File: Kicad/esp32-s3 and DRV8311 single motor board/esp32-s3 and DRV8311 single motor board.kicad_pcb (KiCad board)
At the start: 4 copper layers, 38.8 x 42.1 mm, 74 parts, among them J1 JST SH SM04B, J2 JST SH SM06B, J3 Molex_PicoBlade_53048-0310 Ho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, J4 Conn_01x02_Pin, Q1 NMOS, sir404dp, Q2 NMOS, Q3 PMOS,Si7157DP, Q4 PMOS, SW1 SW_Push, U1 STM32G070CBTr, U2 DRV8311HRRWR, U3 BQ298012RUGT, U4 BQ25060, Y1 ABM8-16.000MHZ-10-1-U-T

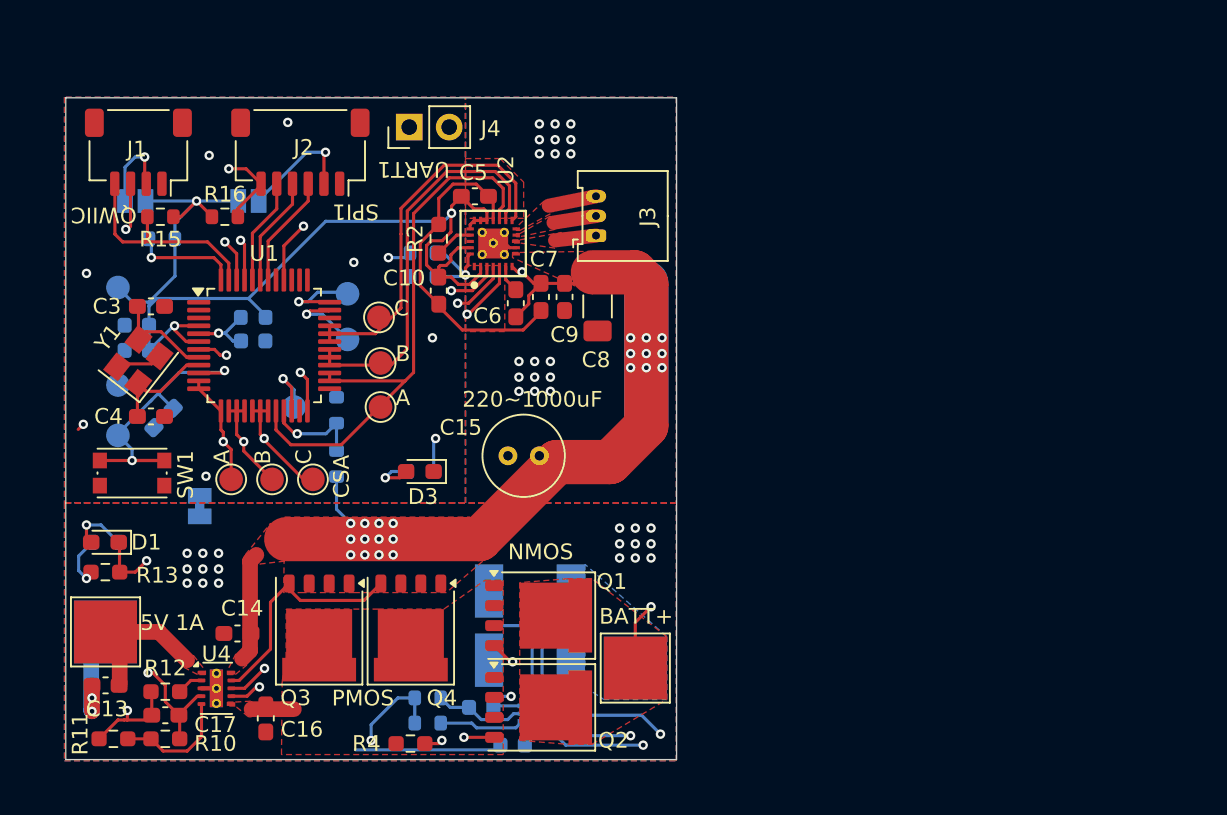
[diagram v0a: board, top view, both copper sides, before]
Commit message: Finished schematic and fixed DRC errors
Now I'm moving on to layout.
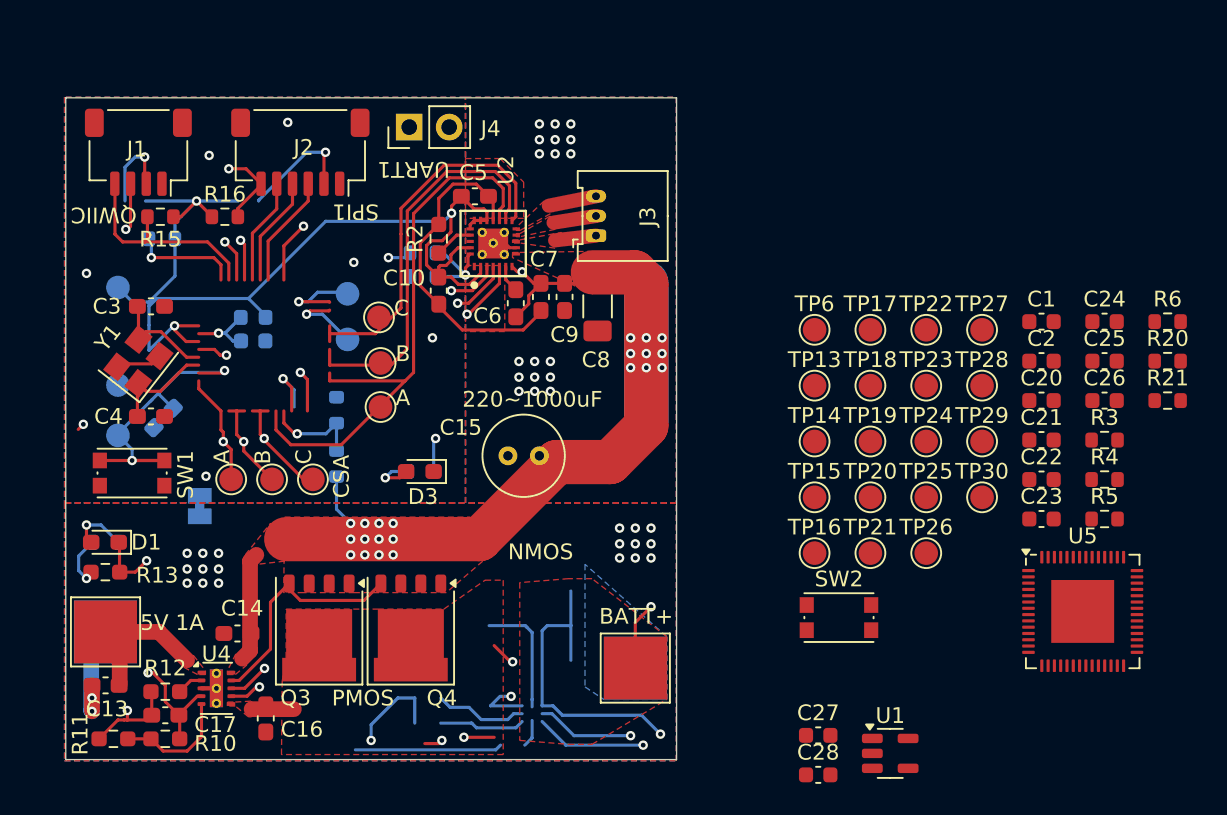
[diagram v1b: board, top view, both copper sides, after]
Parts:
- removed C11: 8nF, Capacitor_SMD:C_0603_1608Metric
- removed C12: 1uF, 16v, Capacitor_SMD:C_0603_1608Metric
- removed JP1, JP2: VCC, Jumper:SolderJumper-2_P1.3mm_Bridged_Pad1.0x1.5mm
- removed Q1: NMOS, sir404dp, Package_DFN_QFN:PQFN-8-EP_6x5mm_P1.27mm_Generic
- removed Q2: NMOS, Package_DFN_QFN:PQFN-8-EP_6x5mm_P1.27mm_Generic
- removed R7: Vishay WSLF2512, 1%, 300uOhm, vishay_wslf:RES_WSLF2512_VIS-M
- removed U3: BQ298012RUGT, bq298rugt:RUG8_TEX
- added C20: 0.1uF, Capacitor_SMD:C_0603_1608Metric, F.Cu at (184.7, 107.4)
- added C21: 1uF, Capacitor_SMD:C_0603_1608Metric, F.Cu at (184.7, 109.9)
- added C22: 0.1uF, Capacitor_SMD:C_0603_1608Metric, F.Cu at (184.7, 112.4)
- added C23: 0.1uF, Capacitor_SMD:C_0603_1608Metric, F.Cu at (184.7, 114.9)
- added C24: 1uF, Capacitor_SMD:C_0603_1608Metric, F.Cu at (188.7, 102.4)
- added C25: 0.1uF, Capacitor_SMD:C_0603_1608Metric, F.Cu at (188.7, 104.9)
- added C26: 22uF, Capacitor_SMD:C_0603_1608Metric, F.Cu at (188.7, 107.4)
- added C27: 22uf, Capacitor_SMD:C_0603_1608Metric, F.Cu at (170.5, 128.7)
- added C28: 22uf, Capacitor_SMD:C_0603_1608Metric, F.Cu at (170.5, 131.2)
- added R20: 10k, Resistor_SMD:R_0603_1608Metric, F.Cu at (192.8, 104.9)
- added R21: 100k, Resistor_SMD:R_0603_1608Metric, F.Cu at (192.8, 107.4)
- added SW2: SW_Push, Button_Switch_SMD:SW_Push_1P1T_NO_CK_KMR2, F.Cu at (171.8, 121.2)
- added TP13: TestPoint, TestPoint:TestPoint_Pad_D1.5mm, F.Cu at (170.3, 106.4)
- added TP14: ~, TestPoint:TestPoint_Pad_D1.5mm, F.Cu at (170.3, 110.0)
- added TP15: ~, TestPoint:TestPoint_Pad_D1.5mm, F.Cu at (170.3, 113.5)
- added TP16: ~, TestPoint:TestPoint_Pad_D1.5mm, F.Cu at (170.3, 117.1)
- added TP17: ~, TestPoint:TestPoint_Pad_D1.5mm, F.Cu at (173.8, 102.9)
- added TP18: ~, TestPoint:TestPoint_Pad_D1.5mm, F.Cu at (173.8, 106.4)
- added TP19: ~, TestPoint:TestPoint_Pad_D1.5mm, F.Cu at (173.8, 110.0)
- added TP20: ~, TestPoint:TestPoint_Pad_D1.5mm, F.Cu at (173.8, 113.5)
- added TP21: ~, TestPoint:TestPoint_Pad_D1.5mm, F.Cu at (173.8, 117.1)
- added TP22: ~, TestPoint:TestPoint_Pad_D1.5mm, F.Cu at (177.4, 102.9)
- added TP23: ~, TestPoint:TestPoint_Pad_D1.5mm, F.Cu at (177.4, 106.4)
- added TP24: ~, TestPoint:TestPoint_Pad_D1.5mm, F.Cu at (177.4, 110.0)
- added TP25: ~, TestPoint:TestPoint_Pad_D1.5mm, F.Cu at (177.4, 113.5)
- added TP26: ~, TestPoint:TestPoint_Pad_D1.5mm, F.Cu at (177.4, 117.1)
- added TP27: ~, TestPoint:TestPoint_Pad_D1.5mm, F.Cu at (180.9, 102.9)
- added TP28: ~, TestPoint:TestPoint_Pad_D1.5mm, F.Cu at (180.9, 106.4)
- added TP29: ~, TestPoint:TestPoint_Pad_D1.5mm, F.Cu at (180.9, 110.0)
- added TP30: ~, TestPoint:TestPoint_Pad_D1.5mm, F.Cu at (180.9, 113.5)
- added U5: ESP32-S3, Package_DFN_QFN:QFN-56-1EP_7x7mm_P0.4mm_EP4x4mm, F.Cu at (187.3, 120.8)
- C1: value 0.1uF -> 1uF; moved to F.Cu
- C18: value 0.1uF -> 1uF
- C2: value 4.7uF -> 1uF; moved to F.Cu
- C3, C4: value 12pF -> 16pF
- J2: value JST SH SM06B -> 7 pin FPC 0.3mm
- R3: value 20ohm -> 33ohm; moved to F.Cu
- R4: value 2k -> 33ohm; footprint Resistor_SMD:R_0603_1608Metric_Pad0.98x0.95mm_HandSolder -> Resistor_SMD:R_0603_1608Metric
- R5: value 300ohm -> 33ohm; moved to F.Cu
- R6: value Same, 1000uOhm -> 33ohm; footprint vishay_wslf:RES_WSLF2512_VIS-M -> Resistor_SMD:R_0603_1608Metric; moved to F.Cu
- TP6: value TestPoint -> ~; moved to F.Cu
- U1: value STM32G070CBTr -> AP2112K-3.3; footprint Package_QFP:LQFP-48_7x7mm_P0.5mm -> Package_TO_SOT_SMD:SOT-23-5
- Y1: value ABM8-16.000MHZ-10-1-U-T -> 40mhz, 10ppm
- moved C2 57.6 mm to (184.7, 104.9), turned to 0 degrees
- moved C1 57.6 mm to (184.7, 102.4), turned to 0 degrees
- moved U1 47.5 mm to (175.1, 129.8)
- moved R4 47.2 mm to (188.7, 112.4)
- moved R3 46.7 mm to (188.7, 109.9)
- moved R5 44.5 mm to (188.7, 114.9)
- moved R6 44.0 mm to (192.8, 102.4), turned to 0 degrees
- moved TP6 33.5 mm to (170.3, 102.9), turned to 0 degrees
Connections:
- C10 pad 2: VDD -> /DRV8311/RegulatorOut
- C16 pad 2: /PSU/Pack+ -> /PSU/BATT+
- C19 pad 1: GND -> Net-(C19-Pad1)
- C19 pad 2: Net-(U1-VREF+) -> GND
- C3 pad 1: Net-(U1-PF0) -> Net-(U5-XTAL_P)
- C4 pad 1: Net-(U1-PF1) -> Net-(U5-XTAL_N)
- C5 pad 2: VDD -> /DRV8311/RegulatorOut
- FB1 pad 1: Net-(U1-VREF+) -> Net-(C19-Pad1)
- H2 pad 1: /PSU/BATT- -> GNDPWR
- J1 pad 2: Net-(J1-Pin_2) -> VDD
- J2 pad 2: Net-(J2-Pin_2) -> VDD
- J4 pad 1: /USART1_TX -> /UART0_TX
- J4 pad 2: /USART1_RX -> /UART0_RX
- Q3 pad 5: /PSU/Pack+ -> /PSU/BATT+
- Q4 pad 5: /PSU/Pack+ -> /PSU/BATT+
- R17 pad 1: /ADC10/VBATT -> /VBATT
- R18 pad 2: /ADC10/VBATT -> /VBATT
- R3 pad 1: /PSU/BATT+ -> Net-(U5-MTDI)
- R3 pad 2: Net-(U3-BAT) -> /MISO1
- R4 pad 1: /PSU/Pack+ -> Net-(U5-MTDO)
- R4 pad 2: Net-(U3-PACK) -> /MOSI1
- R5 pad 1: /PSU/BATT+ -> Net-(U5-MTCK)
- R5 pad 2: Net-(U3-VDD) -> /SCK1
- R6 pad 1: /PSU/BATT- -> /CS1
- R6 pad 2: GNDPWR -> Net-(U5-GPIO12)
- TP1 pad 1: /NRST -> /CS0
- TP2 pad 1: /SWD -> /SCK1
- TP3 pad 1: /SWC -> /MOSI1
- TP6 pad 1: /ADC11 -> Net-(U5-SPICLK_P)
- U1 pad 1: /CS2 -> /MOTORPWR
- U1 pad 2: /CS3 -> GND
- U1 pad 3: /CS4 -> /MOTORPWR
- U1 pad 4: VDD -> unconnected-(U1-NC-Pad4)
- U1 pad 5: Net-(U1-VREF+) -> VDD
- U2 pad 17: VDD -> /DRV8311/RegulatorOut
- U2 pad 18: VDD -> /DRV8311/RegulatorOut
- U2 pad 19: VDD -> /DRV8311/RegulatorOut
- U2 pad 2: VDD -> /DRV8311/RegulatorOut
- U2 pad 20: VDD -> /DRV8311/RegulatorOut
- U2 pad 23: VDD -> /DRV8311/RegulatorOut
- U4 pad 6: /PSU/Pack+ -> /PSU/BATT+
- Y1 pad 1: Net-(U1-PF1) -> Net-(U5-XTAL_N)
- Y1 pad 3: Net-(U1-PF0) -> Net-(U5-XTAL_P)
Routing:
- net (no net): track 0.00 -> 69.5 mm, vias 0 -> 6
- net /PSU/BATT-: track 34.2 -> 0.00 mm, vias 2 -> 0
- net GNDPWR: track 26.1 -> 60.3 mm, vias 38 -> 40
- net Net-(Q1-G): track 27.7 -> 0.00 mm, vias 3 -> 0
- net /USART1_RX: track 20.4 -> 0.00 mm, vias 1 -> 0
- net /UART0_RX: track 0.00 -> 20.4 mm, vias 0 -> 1
- net Net-(U3-PACK): track 20.0 -> 0.00 mm, vias 2 -> 0
- net /USART1_TX: track 17.5 -> 0.00 mm, vias 1 -> 0
- net /UART0_TX: track 0.00 -> 17.5 mm, vias 0 -> 1
- net VDD: track 69.7 -> 82.8 mm, vias 3 -> 5
- net Net-(J2-Pin_2): track 7.60 -> 0.00 mm, vias 1 -> 0
- net Net-(U5-XTAL_P): track 0.00 -> 7.05 mm
- net Net-(U1-PF0): track 7.05 -> 0.00 mm
- net Net-(U5-XTAL_N): track 0.00 -> 6.88 mm
- net Net-(U1-PF1): track 6.88 -> 0.00 mm
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- removed copper zone on B.Cu, net /PSU/BATT-
- removed copper zone on F.Cu, net /PSU/Pack+

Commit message: Wired decoupling capacitors and crystal
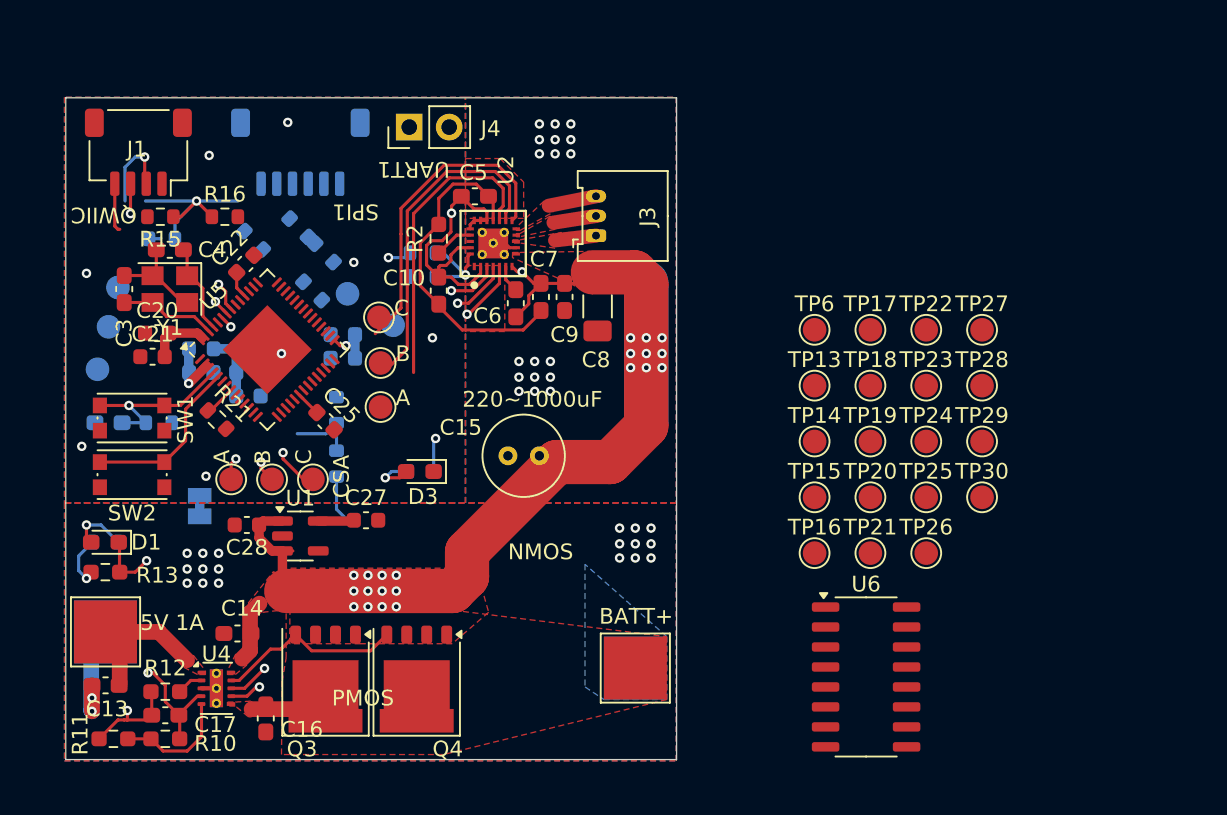
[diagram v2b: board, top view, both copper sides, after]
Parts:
- added U6: 74HC595, Package_SO:SO-16_3.9x9.9mm_P1.27mm, F.Cu at (173.6, 125.0)
- C1, C2, C23, C24, C26, J2, R20, R3, R4, R5, R6: moved to B.Cu
- Y1: footprint Crystal:Crystal_SMD_Abracon_ABM8G-4Pin_3.2x2.5mm -> Crystal:Crystal_SMD_3225-4Pin_3.2x2.5mm
- moved R20 64.3 mm to (128.6, 108.8)
- moved R21 60.5 mm to (132.3, 108.6), turned to -45 degrees
- moved C21 56.8 mm to (128.2, 104.6)
- moved C20 56.4 mm to (128.5, 103.1)
- moved R3 55.6 mm to (134.6, 97.2), turned to 135 degrees
- moved R6 55.6 mm to (137.5, 96.4), turned to 135 degrees
- moved U5 54.5 mm to (135.5, 104.2), turned to 45 degrees
- moved C26 54.4 mm to (134.3, 107.1)
- moved C22 52.5 mm to (134.1, 98.7), turned to 45 degrees
- moved R5 52.4 mm to (138.4, 100.4), turned to 135 degrees
- moved R4 51.7 mm to (139.1, 98.0), turned to 135 degrees
- moved C1 50.5 mm to (134.3, 104.1)
- moved C2 50.4 mm to (134.3, 105.6)
- moved C25 49.7 mm to (139.2, 108.7), turned to -45 degrees
- moved C24 48.5 mm to (140.3, 104.7), turned to 180 degrees
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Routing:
- net (no net): track 69.5 -> 0.00 mm, vias 6 -> 0
- net GNDPWR: track 60.3 -> 9.07 mm, vias 40 -> 38
- net VDD: track 82.8 -> 34.9 mm, vias 5 -> 3
- net /PSU/BATT+: track 34.5 -> 2.69 mm, vias 2 -> 0
- net /DRV8311/RegulatorOut: track 0.00 -> 17.7 mm, vias 0 -> 1
- net /1A: track 36.7 -> 19.2 mm
- net /CS1: track 15.4 -> 0.00 mm, vias 2 -> 0
- net /SCK1: track 12.0 -> 0.00 mm, vias 1 -> 0
- net /MOSI1: track 12.1 -> 0.14 mm, vias 1 -> 0
- net Net-(U5-GPIO0): track 0.00 -> 10.9 mm
- net /SCL1: track 14.1 -> 3.25 mm
- net /SDA1: track 12.5 -> 5.38 mm, vias 2 -> 1
- net /1CSA-A: track 34.3 -> 27.3 mm
- net /1CSA-C: track 31.7 -> 24.7 mm
- net /MISO1: track 6.97 -> 0.00 mm
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
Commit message: Wiring some signal wires and moving power around to accomodate
There are location conflicts left and right! I will eventually get this mess sorted out, but I am wondering about 6 layer boards and blind vias. 4 layers will keep the costs down though!
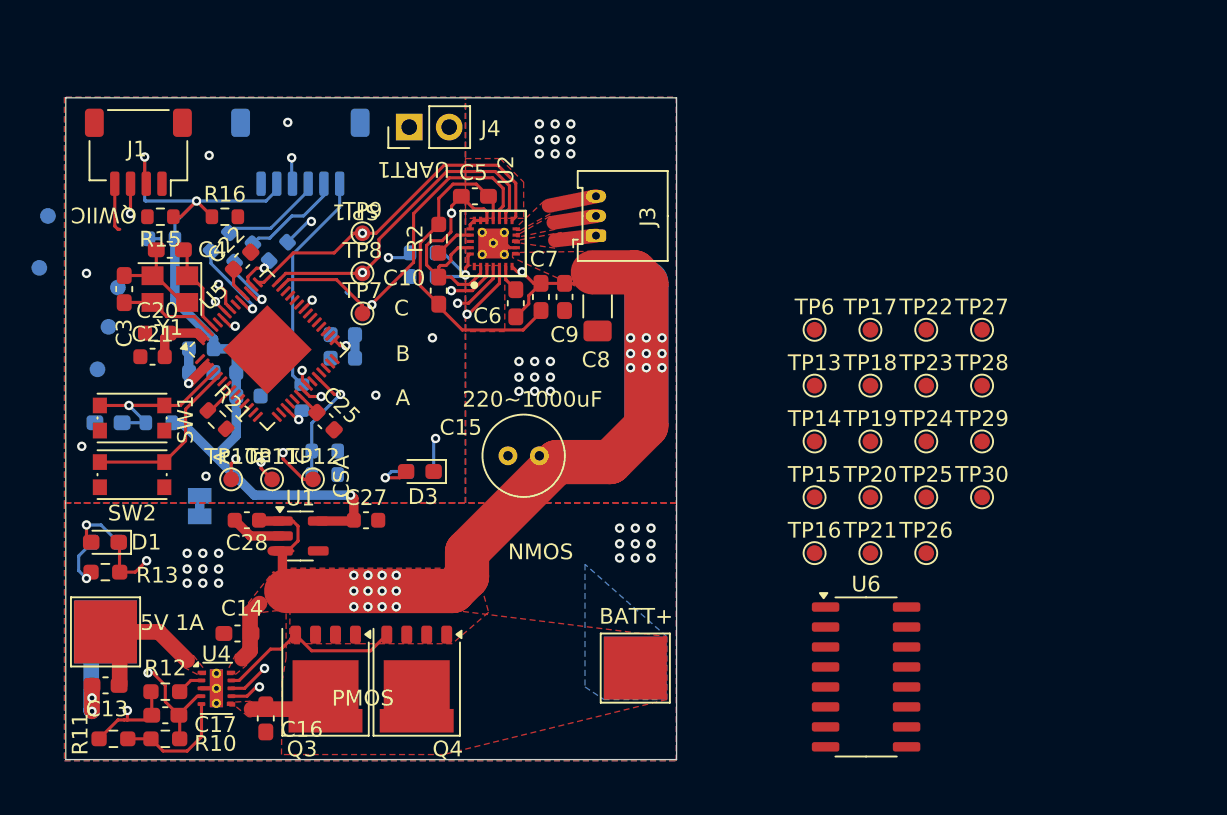
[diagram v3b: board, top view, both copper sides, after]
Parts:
- TP1, TP10, TP11, TP12, TP13, TP14, TP15, TP16, TP17, TP18, TP19, TP2, TP20, TP21, TP22, TP23, TP24, TP25, TP26, TP27, TP28, TP29, TP3, TP30, TP4, TP5, TP6, TP7, TP8, TP9: footprint TestPoint:TestPoint_Pad_D1.5mm -> TestPoint:TestPoint_Pad_D1.0mm
- moved TP2 23.0 mm to (121.5, 95.7)
- moved TP3 19.7 mm to (121.0, 99.0)
- moved R6 10.8 mm to (137.7, 107.2), turned to -90 degrees
- moved TP7 6.06 mm to (141.6, 101.8)
- moved TP8 5.81 mm to (141.6, 99.3)
- moved TP9 5.45 mm to (141.6, 96.8)
- moved R4 5.12 mm to (134.0, 98.0), turned to 45 degrees
- moved R5 3.33 mm to (136.2, 97.9), turned to 45 degrees
- moved R18 2.71 mm to (139.2, 110.6), turned to 180 degrees
- moved R3 2.13 mm to (132.5, 97.3), turned to 45 degrees
- moved R17 1.03 mm to (139.2, 112.1), turned to 0 degrees
- moved C28 0.30 mm to (134.2, 115.0)
- moved C22 0.28 mm to (133.9, 98.5)
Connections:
- U2 pad 10: Net-(J3-Pin_1) -> Net-(J3-Pin_3)
- U2 pad 12: Net-(J3-Pin_3) -> Net-(J3-Pin_1)
- U5 pad 41: /1C -> /1A
- U5 pad 43: /1A -> /1C
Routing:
- net VDD: track 34.9 -> 64.9 mm, vias 3 -> 4
- net /CS1: track 0.00 -> 14.3 mm
- net /1A: track 19.2 -> 32.6 mm, vias 0 -> 2
- net /LED: track 13.5 -> 3.19 mm
- net /1B: track 20.4 -> 30.2 mm, vias 0 -> 2
- net /1C: track 20.0 -> 28.8 mm, vias 0 -> 2
- net /SCK1: track 0.00 -> 8.64 mm, vias 0 -> 2
- net /MISO1: track 0.00 -> 6.57 mm
- net /MOSI1: track 0.14 -> 6.68 mm
- net Net-(U5-MTDI): track 0.00 -> 5.79 mm, vias 0 -> 1
- net Net-(U5-MTDO): track 0.00 -> 4.13 mm, vias 0 -> 1
- net GND: track 63.5 -> 66.9 mm, vias 10 -> 9
- net /VBATT: track 4.53 -> 7.82 mm, vias 0 -> 1
- net Net-(U5-MTCK): track 0.00 -> 2.67 mm, vias 0 -> 1
- net /MOTORPWR: track 128.2 -> 126.1 mm
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
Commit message: Wire mess progress
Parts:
- U6: footprint Package_SO:SO-16_3.9x9.9mm_P1.27mm -> Package_DFN_QFN:DHVQFN-16-1EP_2.5x3.5mm_P0.5mm_EP1x2mm
- moved TP30 50.3 mm to (135.1, 92.9)
- moved TP29 48.0 mm to (136.7, 91.3)
- moved U6 46.7 mm to (138.4, 94.2), turned to -90 degrees
- moved TP26 46.6 mm to (139.8, 89.5)
- moved TP28 46.4 mm to (137.8, 89.5)
- moved TP27 43.8 mm to (138.8, 91.3)
- moved TP25 42.8 mm to (140.8, 91.3)
- moved TP24 39.1 mm to (142.3, 92.8)
- moved TP23 36.9 mm to (142.3, 94.8)
- moved TP13 11.5 mm to (179.8, 113.0)
- moved L1 3.20 mm to (128.0, 114.1)
- moved R16 1.02 mm to (132.6, 96.7), turned to 90 degrees
- moved R21 0.76 mm to (132.9, 109.0)
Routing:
- net /SCL1: track 3.25 -> 25.7 mm, vias 0 -> 2
- net /SDA1: track 5.38 -> 21.3 mm, vias 1 -> 2
- net Net-(U5-GPIO35): track 0.00 -> 8.49 mm, vias 0 -> 2
- net /1CSA-B: track 25.5 -> 33.0 mm
- net Net-(U5-GPIO33): track 0.00 -> 6.73 mm, vias 0 -> 2
- net /1CSA-A: track 27.3 -> 33.8 mm
- net Net-(U5-GPIO34): track 0.00 -> 6.24 mm, vias 0 -> 2
- net /1CSA-C: track 24.7 -> 30.4 mm
- net Net-(U6-QD): track 0.00 -> 3.73 mm
- net Net-(U6-QF): track 0.00 -> 3.68 mm
- net Net-(U6-QA): track 0.00 -> 2.93 mm
- net Net-(U6-QB): track 0.00 -> 2.75 mm
- net Net-(U6-QC): track 0.00 -> 2.18 mm
- net Net-(U6-QH): track 0.00 -> 2.16 mm
- net Net-(U6-QG): track 0.00 -> 2.11 mm
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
